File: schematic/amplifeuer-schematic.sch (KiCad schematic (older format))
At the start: 16 parts, among them J1 Input, J3 Output1, J4 Output2, J5 Power, U1 TDA1521A

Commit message: Move amplifier schematic 1 layer down
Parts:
- removed C1, C2: 220nF, Capacitor_THT:C_Disc_D5.0mm_W2.5mm_P5.00mm, symbol Device:C
- removed C3, C6, C7: 680μF, Capacitor_THT:CP_Radial_D10.0mm_P5.00mm, symbol Device:CP
- removed C4, C5: 22nF, Capacitor_THT:C_Disc_D3.4mm_W2.1mm_P2.50mm, symbol Device:C
- removed C8: 100nF, Capacitor_THT:C_Disc_D7.5mm_W2.5mm_P5.00mm, symbol Device:C
- removed C9: 100μF, Capacitor_THT:CP_Radial_D8.0mm_P2.50mm, symbol Device:CP
- removed J1: Input, Connector_PinHeader_2.54mm:PinHeader_1x03_P2.54mm_Vertical, symbol Connector:Conn_01x03_Male
- removed J3: Output1, Connector_PinHeader_2.54mm:PinHeader_1x02_P2.54mm_Vertical, symbol Connector:Conn_01x02_Male
- removed J4: Output2, Connector_PinHeader_2.54mm:PinHeader_1x02_P2.54mm_Vertical, symbol Connector:Conn_01x02_Male
- removed J5: Power, Connector_PinHeader_2.54mm:PinHeader_1x02_P2.54mm_Vertical, symbol Connector:Conn_01x02_Male
- removed R1, R2: 10R, Resistor_THT:R_Axial_DIN0411_L9.9mm_D3.6mm_P15.24mm_Horizontal, symbol Device:R
- removed U1: TDA1521A, symbol TDA1521A:TDA1521A
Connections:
- net labels removed: +12V, GND
- wire segments 23 -> 0

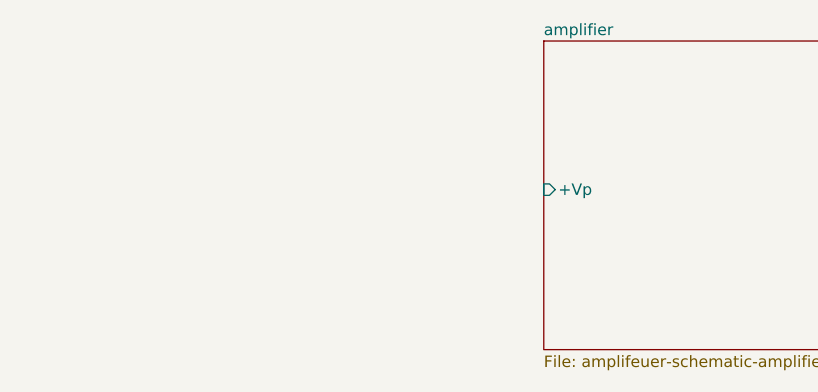
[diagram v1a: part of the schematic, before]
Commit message: Add rudimentary PSU schematic and layout
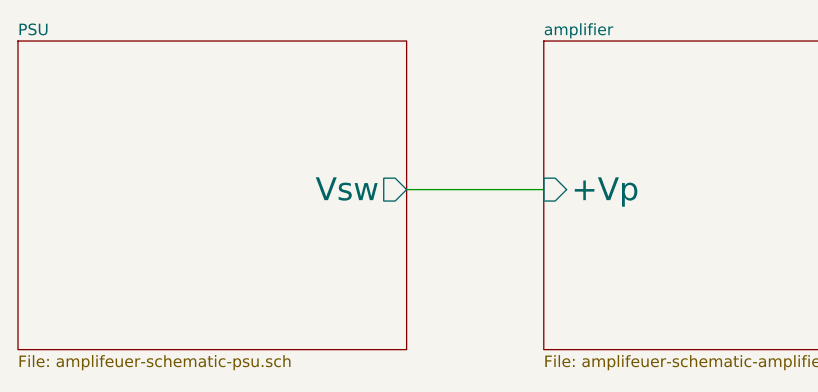
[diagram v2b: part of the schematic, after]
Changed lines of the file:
@@
 $Descr A4 11693 8268
 encoding utf-8
-Sheet 1 2
+Sheet 1 3
 Title "amplifeuer"
 Date "2019-08-05"
@@
 F0 "amplifier" 50
 F1 "amplifeuer-schematic-amplifier.sch" 50
-F2 "+Vp" I L 8400 3550 50
+F2 "+Vp" I L 8400 3550 100
 $EndSheet
+$Sheet
+S 6100 2900 1700 1350
+U 5D49AD36
+F0 "PSU" 50
+F1 "amplifeuer-schematic-psu.sch" 50
+F2 "Vsw" O R 7800 3550 100
+$EndSheet
+Wire Wire Line
+	8400 3550 7800 3550
 $EndSCHEMATC
